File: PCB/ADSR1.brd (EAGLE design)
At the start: 100 x 80 mm, 48 parts, among them IC1 78L05, IC2 4066D, IC3 MCP6002, IC4 TL072D, SW1 TL2285, T1 BC847

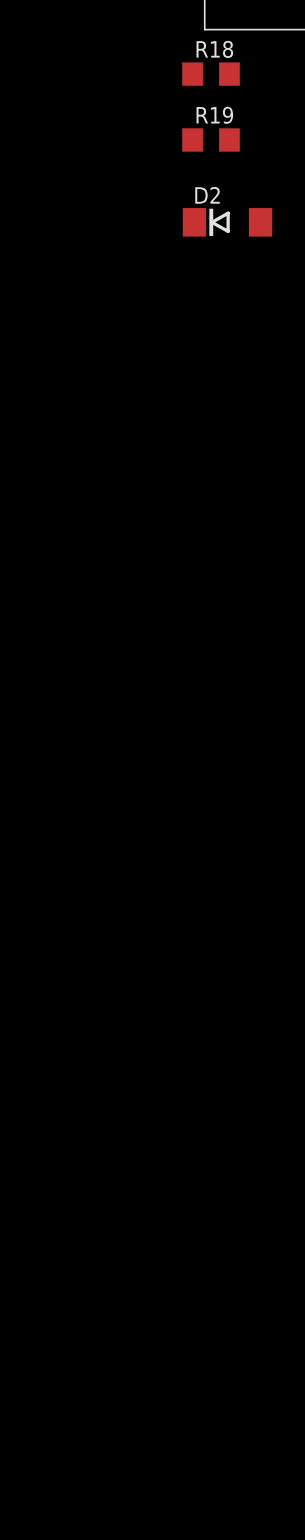
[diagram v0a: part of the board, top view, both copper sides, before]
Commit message: More or less working breadboard prototype. Will probably not do more with this in a while (if ever).
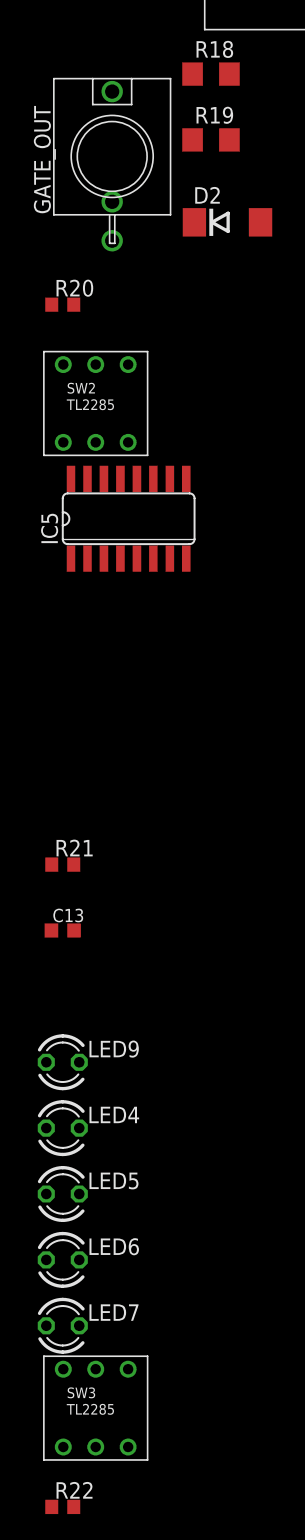
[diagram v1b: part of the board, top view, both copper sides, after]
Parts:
- added C13: 100n, rcl:C0603K
- added GATE_OUT: WQP-PJ301M-12_JACK, thonkiconn:WQP-PJ301M-12_JACK
- added IC5: 4017D, 40xx:SO16
- added LED4, LED5, LED6, LED7, LED9: (no value), led:LED3MM
- added R20, R21: 1k, rcl:R0603
- added R22: 10k, rcl:R0603
- added SW2, SW3: TL2285, lb_devs:TL2285_PCB
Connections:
- new net GATE_OUT: R20.2, U$1.10
- new net MODE_SW: SW2.3, U$1.11
- new net N$22: IC5.2, LED9.A
- new net N$23: GATE_OUT.P$1, R20.1
- new net N$25: IC5.4, LED4.A
- new net N$26: IC5.7, LED5.A
- new net N$27: IC5.10, LED6.A
- new net N$28: LED4.K, LED5.K, LED6.K, LED7.K, LED9.K, R21.1
- new net N$29: IC5.3, LED7.A
- new net N$30: R22.1, SW3.3
- net +5V: now also C13.1, IC5.16
- net GND: now also C13.2, GATE_OUT.P$3, IC5.13, IC5.8, SW2.2, SW3.2
- net MISO: now also IC5.15
- net MOSI: now also R22.2
- net SCK: now also IC5.14, R21.2
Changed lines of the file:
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@@
 <element name="R19" library="rcl" package="R1206" value="100" x="-107.95" y="-100.33"/>
 <element name="D2" library="diode" package="DO214AA" value="1N4004 equiv" x="-106.68" y="-106.68"/>
+<element name="GATE_OUT" library="thonkiconn" package="WQP-PJ301M-12_JACK" value="WQP-PJ301M-12_JACK" x="-115.57" y="-101.6"/>
+<element name="R20" library="rcl" package="R0603" value="1k" x="-119.38" y="-113.03"/>
+<element name="SW2" library="lb_devs" package="TL2285_PCB" value="TL2285" x="-116.84" y="-120.65"/>
+<element name="IC5" library="40xx" package="SO16" value="4017D" x="-114.3" y="-129.54"/>
+<element name="R21" library="rcl" package="R0603" value="1k" x="-119.38" y="-156.21"/>
+<element name="C13" library="rcl" package="C0603K" value="100n" x="-119.38" y="-161.29"/>
+<element name="LED9" library="led" package="LED3MM" value="" x="-119.38" y="-171.45"/>
+<element name="LED4" library="led" package="LED3MM" value="" x="-119.38" y="-176.53"/>
+<element name="LED5" library="led" package="LED3MM" value="" x="-119.38" y="-181.61"/>
+<element name="LED6" library="led" package="LED3MM" value="" x="-119.38" y="-186.69"/>
+<element name="LED7" library="led" package="LED3MM" value="" x="-119.38" y="-191.77"/>
+<element name="SW3" library="lb_devs" package="TL2285_PCB" value="TL2285" x="-116.84" y="-198.12"/>
+<element name="R22" library="rcl" package="R0603" value="10k" x="-119.38" y="-205.74"/>
 </elements>
 <signals>
@@
 <contactref element="IC3" pad="8"/>
 <contactref element="C9" pad="1"/>
-<contactref element="IC2" pad="14"/>
-<contactref element="C8" pad="1"/>
 <contactref element="R10" pad="1"/>
 <contactref element="C6" pad="1"/>
 <contactref element="R5" pad="P$1"/>
+<contactref element="IC2" pad="14"/>
+<contactref element="C8" pad="1"/>
+<contactref element="IC5" pad="16"/>
+<contactref element="C13" pad="1"/>
+<wire x1="-120.255" y1="-161.29" x2="-118.745" y2="-126.4666" width="0" layer="19" extent="1-1"/>
+<wire x1="-63.73" y1="-20.32" x2="-118.745" y2="-126.4666" width="0" layer="19" extent="1-1"/>
 <wire x1="-63.08" y1="-15.24" x2="-63.73" y2="-20.32" width="0" layer="19" extent="1-1"/>
 <wire x1="-48.49" y1="17.3" x2="-63.08" y2="-15.24" width="0" layer="19" extent="1-1"/>
@@
 <contactref element="IC3" pad="4"/>
 <contactref element="C9" pad="2"/>
-<contactref element="IC2" pad="7"/>
-<contactref element="C8" pad="2"/>
 <contactref element="LED1" pad="K"/>
 <contactref element="LED2" pad="K"/>
@@
 <contactref element="R17" pad="P$3"/>
 <contactref element="R19" pad="1"/>
+<contactref element="GATE_OUT" pad="P$3"/>
+<contactref element="SW2" pad="2"/>
+<contactref element="IC5" pad="13"/>
+<contactref element="IC2" pad="7"/>
+<contactref element="C8" pad="2"/>
+<contactref element="IC5" pad="8"/>
+<contactref element="C13" pad="2"/>
+<contactref element="SW3" pad="2"/>
+<wire x1="-114.935" y1="-126.4666" x2="-109.855" y2="-132.6134" width="0" layer="19" extent="1-1"/>
+<wire x1="-116.84" y1="-123.65" x2="-114.935" y2="-126.4666" width="0" layer="19" extent="1-1"/>
+<wire x1="-115.57" y1="-108.1" x2="-116.84" y2="-123.65" width="0" layer="19" extent="1-1"/>
+<wire x1="-109.372" y1="-100.33" x2="-115.57" y2="-108.1" width="0" layer="19" extent="1-1"/>
 <wire x1="-91.44" y1="-90.32" x2="-109.372" y2="-100.33" width="0" layer="19" extent="1-1"/>
 <wire x1="-82.97" y1="-85.09" x2="-91.44" y2="-90.32" width="0" layer="19" extent="1-1"/>
@@
 <wire x1="-13.97" y1="29.9466" x2="-29.21" y2="30.48" width="0" layer="19" extent="1-1"/>
 <wire x1="-19.05" y1="52.07" x2="-34.685" y2="52.07" width="0" layer="19" extent="1-1"/>
+<wire x1="-118.505" y1="-161.29" x2="-109.855" y2="-132.6134" width="0" layer="19" extent="1-1"/>
+<wire x1="-116.84" y1="-201.12" x2="-118.505" y2="-161.29" width="0" layer="19" extent="1-1"/>
 </signal>
 <signal name="+12V">
@@
 <contactref element="U$2" pad="4"/>
 <contactref element="U$1" pad="7"/>
+<contactref element="R22" pad="2"/>
+<wire x1="-39.37" y1="20.32" x2="-118.53" y2="-205.74" width="0" layer="19" extent="1-1"/>
 <wire x1="-40.64" y1="28.95" x2="-39.37" y2="20.32" width="0" layer="19" extent="1-1"/>
 </signal>
@@
 <contactref element="U$2" pad="3"/>
 <contactref element="U$1" pad="9"/>
+<contactref element="IC5" pad="14"/>
+<contactref element="R21" pad="2"/>
+<wire x1="-118.53" y1="-156.21" x2="-116.205" y2="-126.4666" width="0" layer="19" extent="1-1"/>
+<wire x1="-39.37" y1="17.78" x2="-116.205" y2="-126.4666" width="0" layer="19" extent="1-1"/>
 <wire x1="-41.91" y1="34.55" x2="-39.37" y2="17.78" width="0" layer="19" extent="1-1"/>
 </signal>
@@
 <contactref element="U$1" pad="8"/>
 <contactref element="U$2" pad="1"/>
+<contactref element="IC5" pad="15"/>
+<wire x1="-41.91" y1="17.78" x2="-117.475" y2="-126.4666" width="0" layer="19" extent="1-1"/>
 <wire x1="-40.64" y1="34.55" x2="-41.91" y2="17.78" width="0" layer="19" extent="1-1"/>
 </signal>
@@
 <wire x1="-26.67" y1="33.02" x2="-26.67" y2="30.48" width="0" layer="19" extent="1-1"/>
 </signal>
+<signal name="GATE_OUT">
+<contactref element="U$1" pad="10"/>
+<contactref element="R20" pad="2"/>
+<wire x1="-43.18" y1="34.55" x2="-118.53" y2="-113.03" width="0" layer="19" extent="1-1"/>
+</signal>
+<signal name="N$23">
+<contactref element="GATE_OUT" pad="P$1"/>
+<contactref element="R20" pad="1"/>
+<wire x1="-115.57" y1="-96.6" x2="-120.23" y2="-113.03" width="0" layer="19" extent="1-1"/>
+</signal>
+<signal name="MODE_SW">
+<contactref element="U$1" pad="11"/>
+<contactref element="SW2" pad="3"/>
+<wire x1="-44.45" y1="34.55" x2="-114.34" y2="-123.65" width="0" layer="19" extent="1-1"/>
+</signal>
+<signal name="N$22">
+<contactref element="IC5" pad="2"/>
+<contactref element="LED9" pad="A"/>
+<wire x1="-120.65" y1="-171.45" x2="-117.475" y2="-132.6134" width="0" layer="19" extent="1-1"/>
+</signal>
+<signal name="N$25">
+<contactref element="IC5" pad="4"/>
+<contactref element="LED4" pad="A"/>
+<wire x1="-120.65" y1="-176.53" x2="-114.935" y2="-132.6134" width="0" layer="19" extent="1-1"/>
+</signal>
+<signal name="N$27">
+<contactref element="IC5" pad="10"/>
+<contactref element="LED6" pad="A"/>
+<wire x1="-120.65" y1="-186.69" x2="-111.125" y2="-126.4666" width="0" layer="19" extent="1-1"/>
+</signal>
+<signal name="N$28">
+<contactref element="R21" pad="1"/>
+<contactref element="LED9" pad="K"/>
+<contactref element="LED4" pad="K"/>
+<contactref element="LED6" pad="K"/>
+<contactref element="LED5" pad="K"/>
+<contactref element="LED7" pad="K"/>
+<wire x1="-118.11" y1="-186.69" x2="-118.11" y2="-191.77" width="0" layer="19" extent="1-1"/>
+<wire x1="-118.11" y1="-181.61" x2="-118.11" y2="-186.69" width="0" layer="19" extent="1-1"/>
+<wire x1="-118.11" y1="-176.53" x2="-118.11" y2="-181.61" width="0" layer="19" extent="1-1"/>
+<wire x1="-118.11" y1="-171.45" x2="-118.11" y2="-176.53" width="0" layer="19" extent="1-1"/>
+<wire x1="-120.23" y1="-156.21" x2="-118.11" y2="-171.45" width="0" layer="19" extent="1-1"/>
+</signal>
+<signal name="N$26">
+<contactref element="IC5" pad="7"/>
+<contactref element="LED5" pad="A"/>
+<wire x1="-120.65" y1="-181.61" x2="-111.125" y2="-132.6134" width="0" layer="19" extent="1-1"/>
+</signal>
+<signal name="N$29">
+<contactref element="IC5" pad="3"/>
+<contactref element="LED7" pad="A"/>
+<wire x1="-120.65" y1="-191.77" x2="-116.205" y2="-132.6134" width="0" layer="19" extent="1-1"/>
+</signal>
+<signal name="N$30">
+<contactref element="SW3" pad="3"/>
+<contactref element="R22" pad="1"/>
+<wire x1="-114.34" y1="-201.12" x2="-120.23" y2="-205.74" width="0" layer="19" extent="1-1"/>
+</signal>
 </signals>
